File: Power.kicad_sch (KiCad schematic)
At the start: 44 parts, among them J5 Conn_01x02, J6 Conn_01x02, Q1 AO3400A, Q2 AO3401A, Q3 AO3401A, U1 TPS55340PWP, U2 BQ24074RGT, U3 TPS62130

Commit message: I was never here
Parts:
- renumbered R9 to R10, R10 to R11, R11 to R12, R12 to R13, R13 to R14, R14 to R15, R15 to R16, R16 to R17, R17 to R18, R18 to R19, R4 to R5, R5 to R6, R6 to R7, R7 to R8, R8 to R9

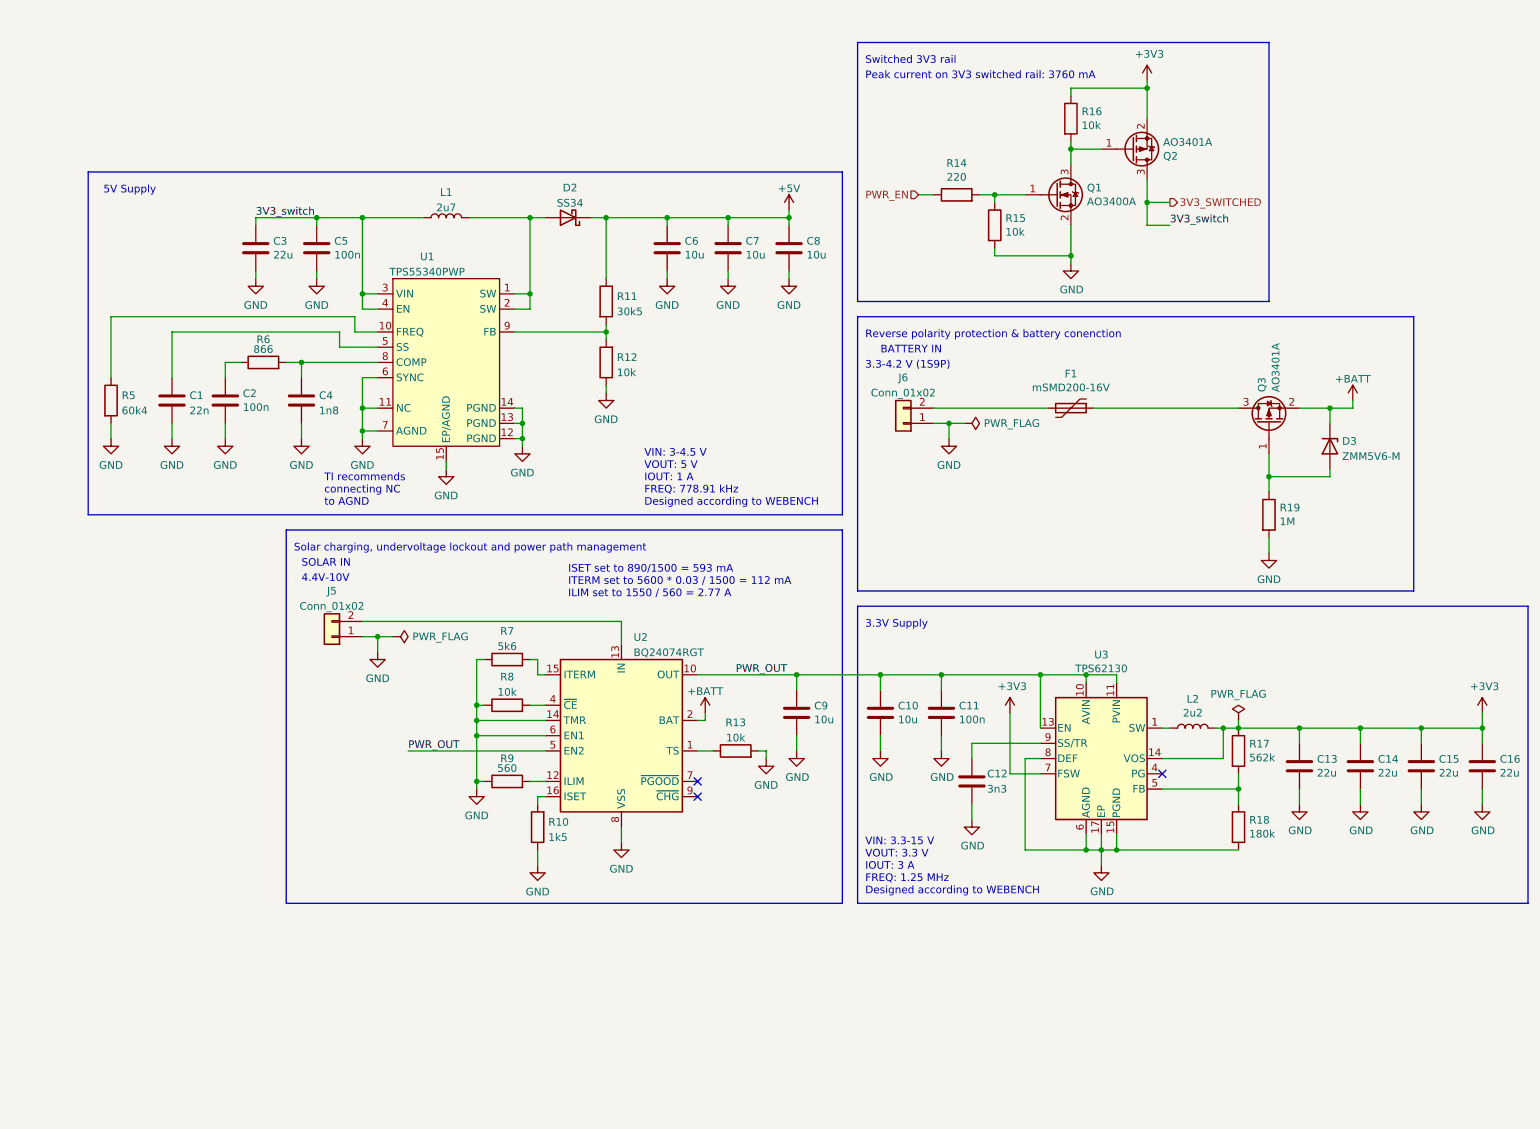
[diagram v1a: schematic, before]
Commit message: Finish routing round 2
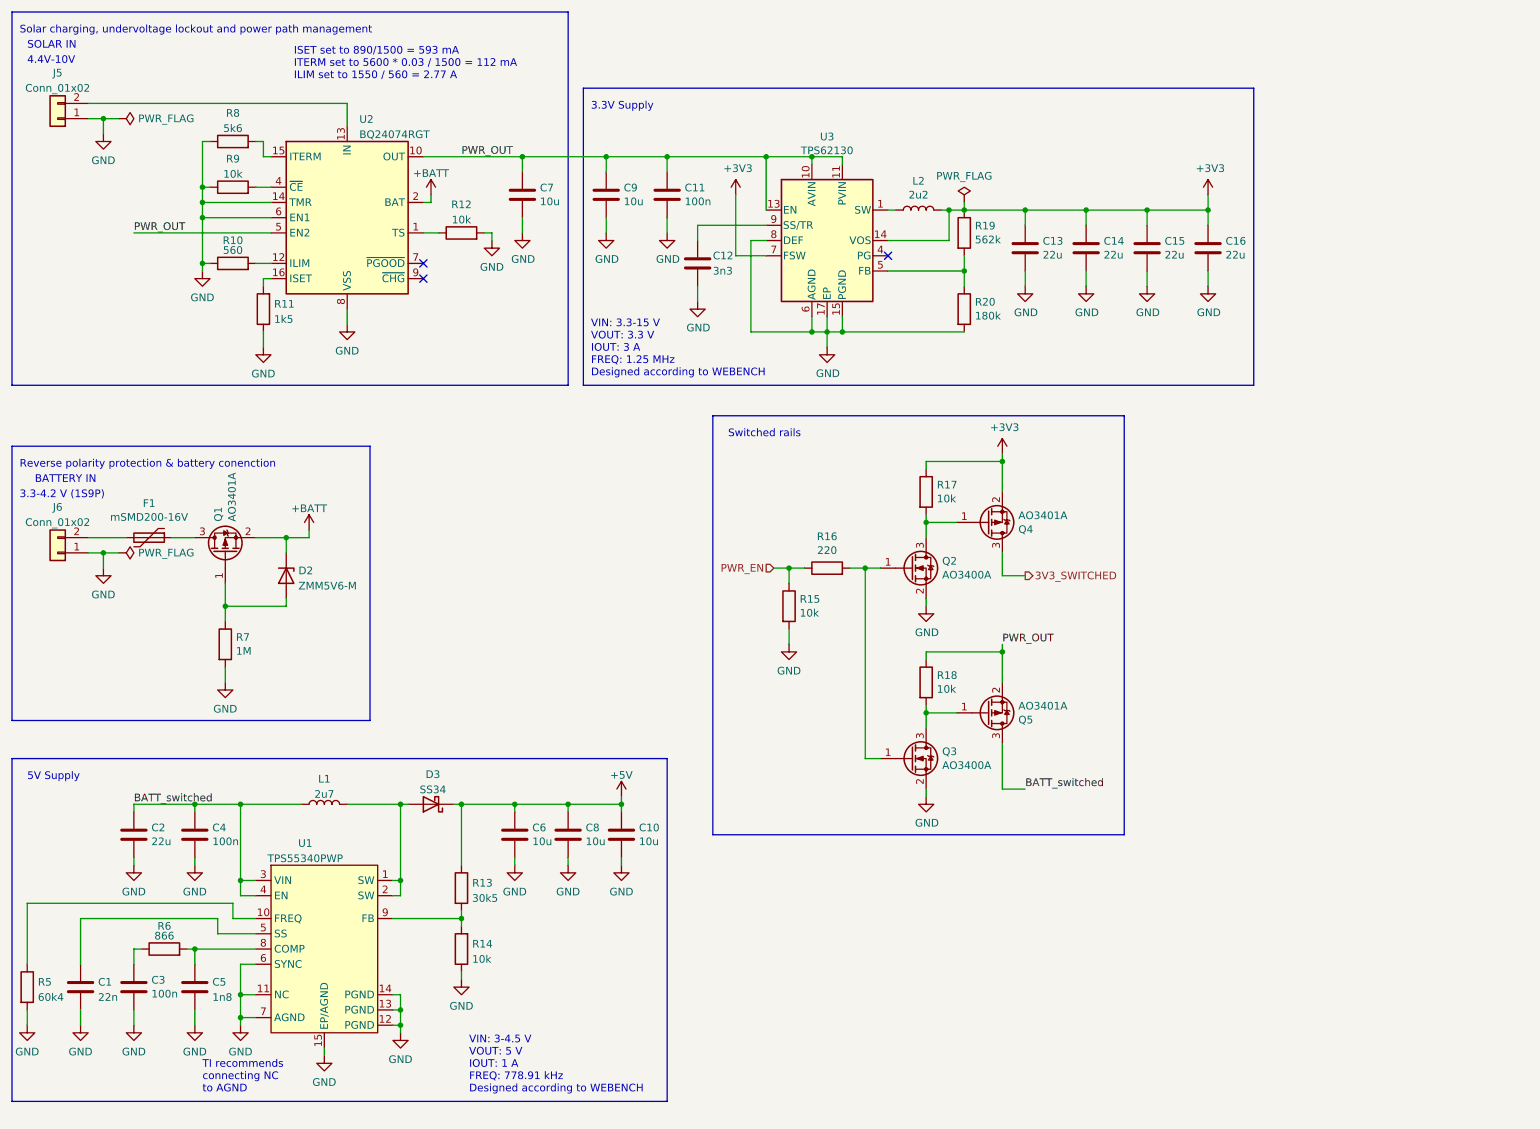
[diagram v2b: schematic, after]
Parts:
- added Q3: AO3400A, Package_TO_SOT_SMD:SOT-23, symbol Transistor_FET:AO3400A
- added Q5: AO3401A, Package_TO_SOT_SMD:SOT-23, symbol Transistor_FET:AO3401A
- added R18: 10k, Resistor_SMD:R_0603_1608Metric, symbol Device:R
- renumbered C8 to C10, C3 to C2, C2 to C3, C5 to C4, C4 to C5, C9 to C7, C7 to C8, C10 to C9, D3 to D2, D2 to D3, Q3 to Q1, Q1 to Q2, Q2 to Q4, R9 to R10, R10 to R11, R13 to R12, R11 to R13, R12 to R14, R14 to R16, R16 to R17, R17 to R19, R18 to R20, R19 to R7, R7 to R8, R8 to R9
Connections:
- net 3V3_SWITCHED: no longer C2.1, C4.1, L1.1, U1.3 (VIN), U1.4 (EN)
- net GND: now also Q3.2 (S)
- net PWR_EN: now also R15.1
- net PWR_OUT: now also Q5.2 (S), R18.1
- net at Q2.1 (G), R16.2: now also Q3.1 (G); no longer R15.1
- new net: Q3.3 (D), Q5.1 (G), R18.2
- new net BATT_switched: C2.1, C4.1, L1.1, Q5.3 (D), U1.3 (VIN), U1.4 (EN)
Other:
- note added: "Switched rails"
- note removed: "Peak current on 3V3 switched rail: 3760 mA"
- note removed: "Switched 3V3 rail"
- moved on the sheet: C1, C10, C11, C12, C13, C14, C15, C16, C2, C3, C4, C5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
